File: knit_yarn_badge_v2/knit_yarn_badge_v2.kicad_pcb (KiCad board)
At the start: 2 copper layers, 33.8 x 36.1 mm, 14 parts, among them SW1 SW_SPST

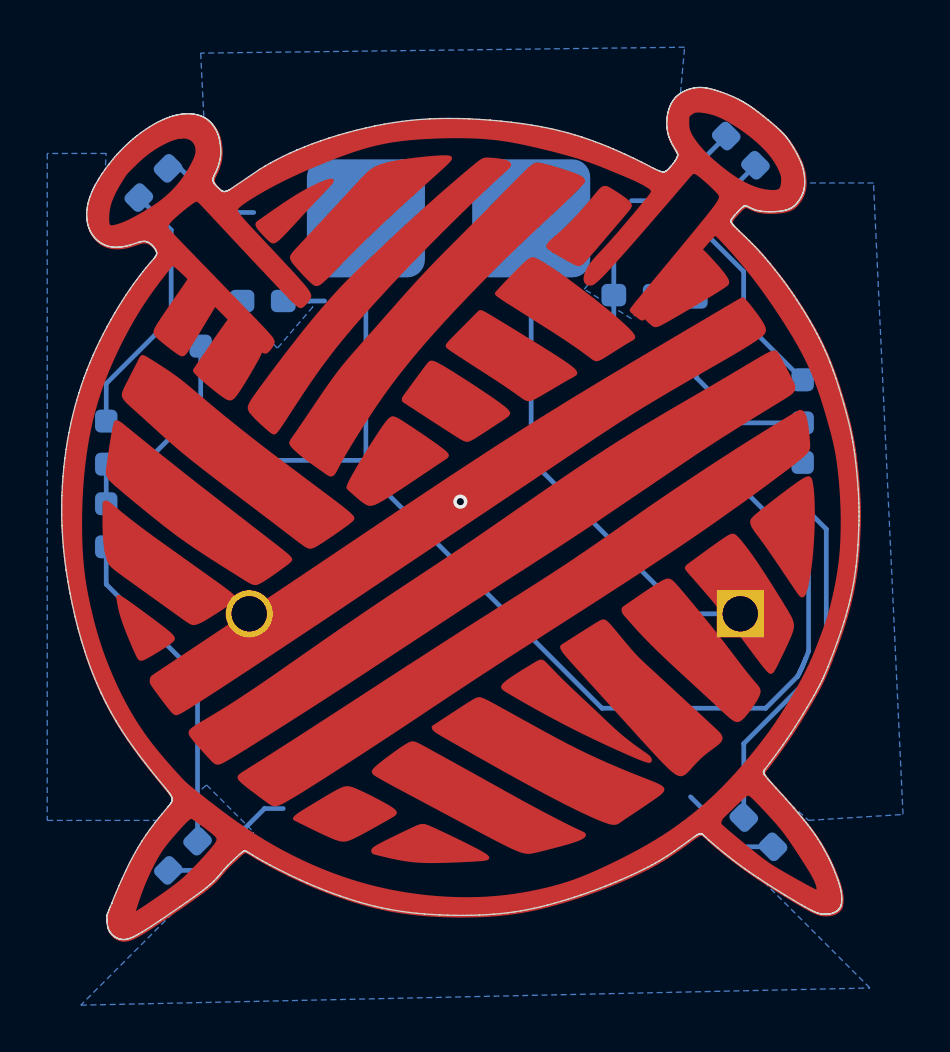
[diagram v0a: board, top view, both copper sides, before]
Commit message: non movable components locked
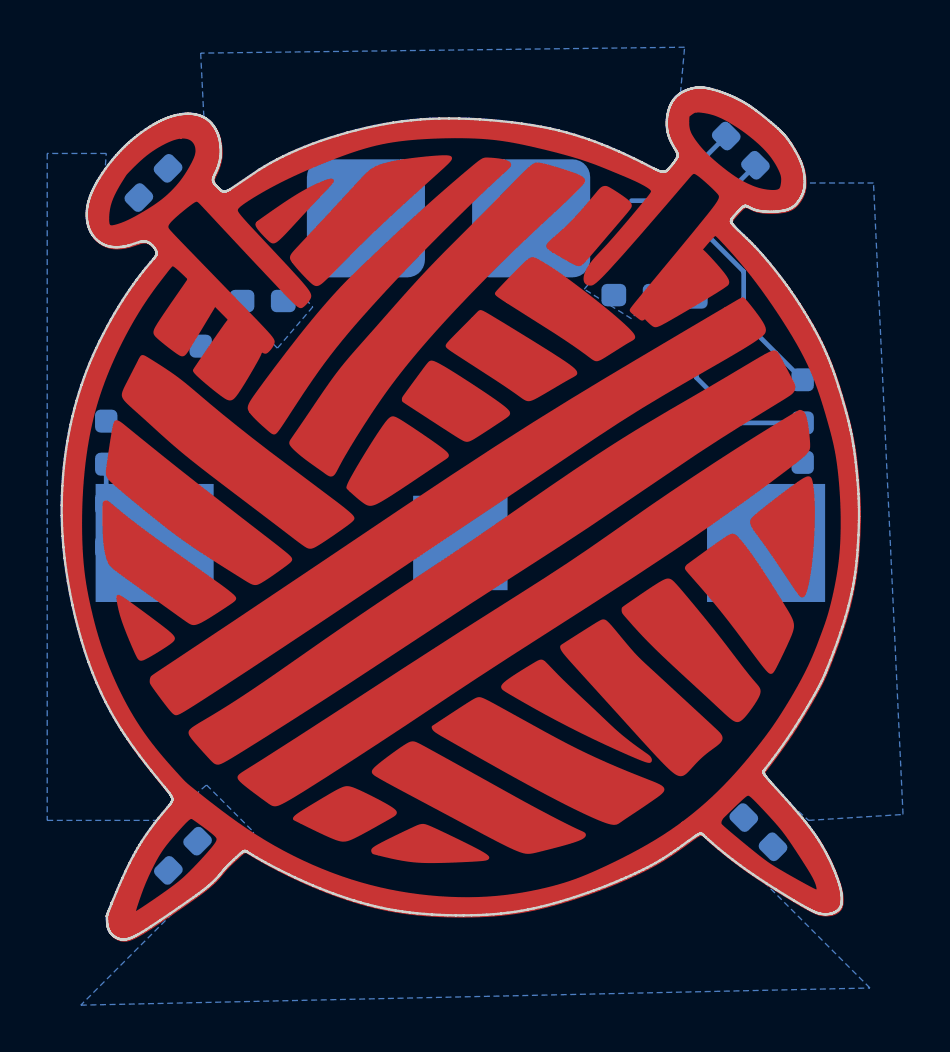
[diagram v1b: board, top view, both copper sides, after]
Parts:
- BT1: footprint Battery:BatteryHolder_MYOUNG_BS-07-A1BJ001_CR2032 -> Battery:BatteryHolder_Multicomp_BC-2001_1x2032
- moved BT1 12.2 mm to (100.0, 90.8), turned to 0 degrees
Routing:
- net +3V0: track 71.5 -> 10.2 mm
- net Net-(BT1-+): track 21.8 -> 0.00 mm
- net GND: track 25.7 -> 5.15 mm, vias 1 -> 0
- net Net-(D1-A): track 14.9 -> 0.00 mm
- net Net-(D2-A): track 14.1 -> 0.00 mm
- net Net-(D4-A): track 11.2 -> 0.00 mm

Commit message: components arranged
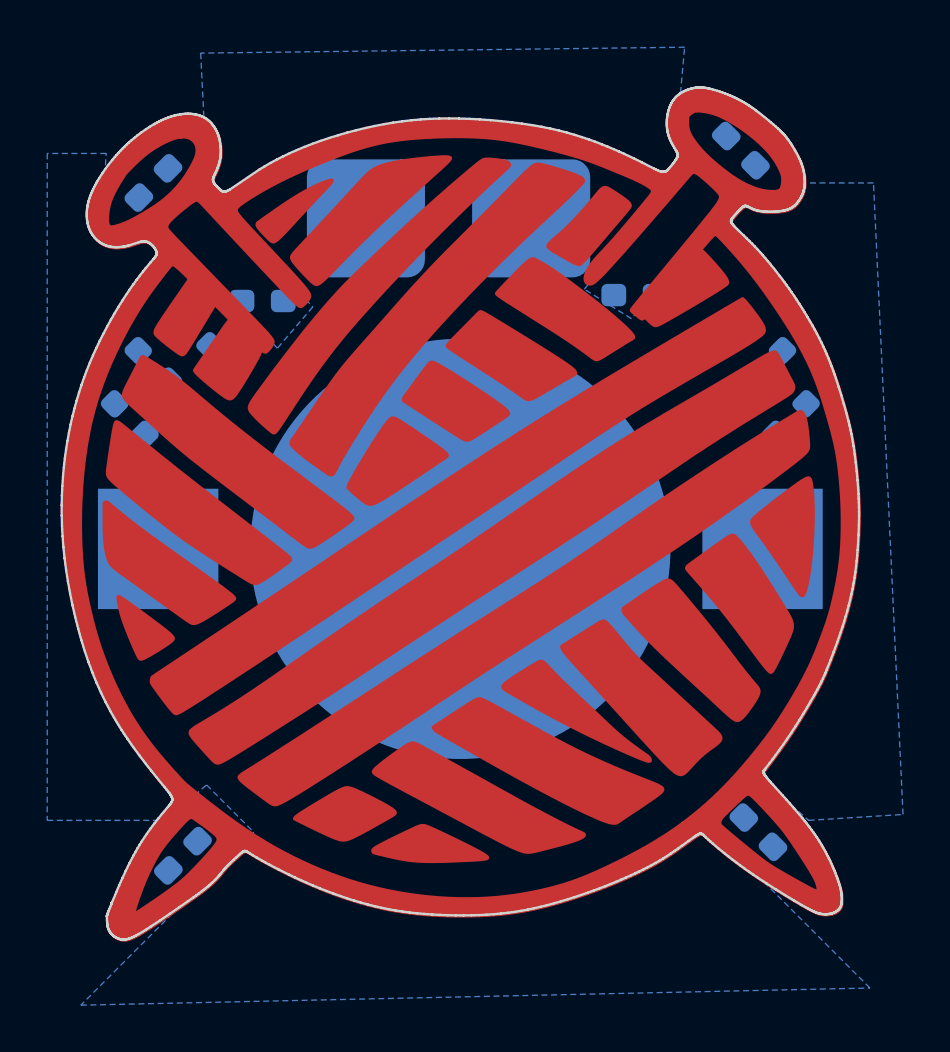
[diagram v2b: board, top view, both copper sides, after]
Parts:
- BT1: footprint Battery:BatteryHolder_Multicomp_BC-2001_1x2032 -> Battery:BatteryHolder_Keystone_3002_1x2032
- moved R2 4.61 mm to (86.0, 85.5), turned to 135 degrees
- moved R4 3.82 mm to (87.0, 83.2), turned to 135 degrees
- moved R1 2.80 mm to (114.0, 85.5), turned to 45 degrees
- moved R3 2.12 mm to (113.0, 83.2), turned to 45 degrees
- moved R5 1.35 mm to (111.2, 81.8), turned to 45 degrees
- moved R6 0.35 mm to (88.8, 81.8), turned to 135 degrees
- moved BT1 0.25 mm to (100.0, 91.0)
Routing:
- net Net-(D3-A): track 11.6 -> 0.00 mm
- net +3V0: track 10.2 -> 0.00 mm
- net GND: track 5.15 -> 0.00 mm
- net Net-(D6-A): track 1.79 -> 0.00 mm
- net Net-(D5-A): track 1.79 -> 0.00 mm
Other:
- board text added: "2025/12/02"
- board text removed: "2025/05/12"

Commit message: everything routed
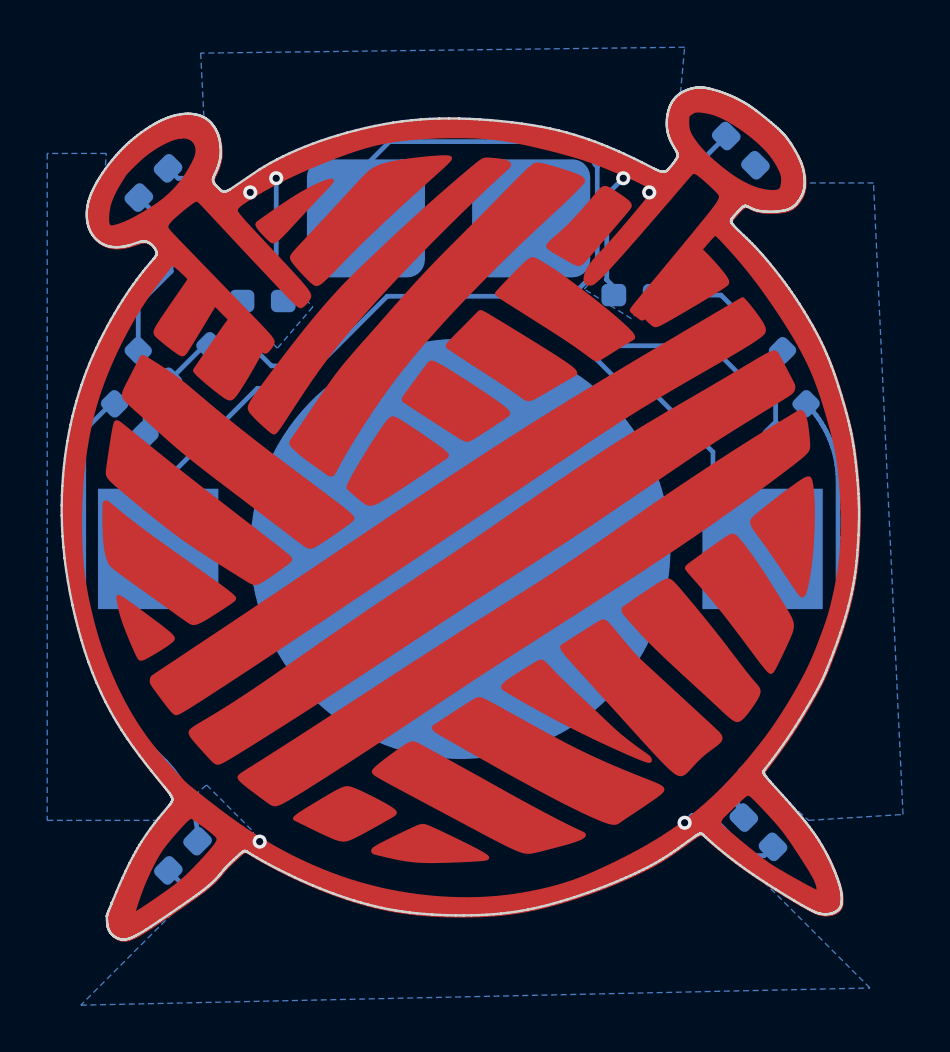
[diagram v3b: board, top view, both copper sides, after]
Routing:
- net +3V0: track 0.00 -> 49.0 mm
- net Net-(BT1-+): track 0.00 -> 40.5 mm
- net GND: track 0.00 -> 29.5 mm, vias 0 -> 6
- net Net-(D2-A): track 0.00 -> 20.4 mm
- net Net-(D1-A): track 0.00 -> 19.1 mm
- net Net-(D4-A): track 0.00 -> 7.63 mm
- net Net-(D5-A): track 0.00 -> 4.00 mm
- net Net-(D6-A): track 0.00 -> 2.90 mm
